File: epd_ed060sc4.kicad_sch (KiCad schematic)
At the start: 13 parts, among them J1 ED060SC4

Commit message: fix paths
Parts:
- J1: footprint (none) -> local_lib:HRS_FH26W-39S-0.3SHW(60)
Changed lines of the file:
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@@
       (effects (font (size 1.27 1.27)) (justify left))
     )
-    (property "Footprint" "" (at 173.99 82.55 0)
+    (property "Footprint" "local_lib:HRS_FH26W-39S-0.3SHW(60)" (at 173.99 82.55 0)
       (effects (font (size 1.27 1.27)) hide)
     )
-    (property "Datasheet" "" (at 173.99 82.55 0)
+    (property "Datasheet" "https://datasheetspdf.com/pdf-file/730402/PrimeView/ED060SC4/1" (at 173.99 82.55 0)
       (effects (font (size 1.27 1.27)) hide)
     )

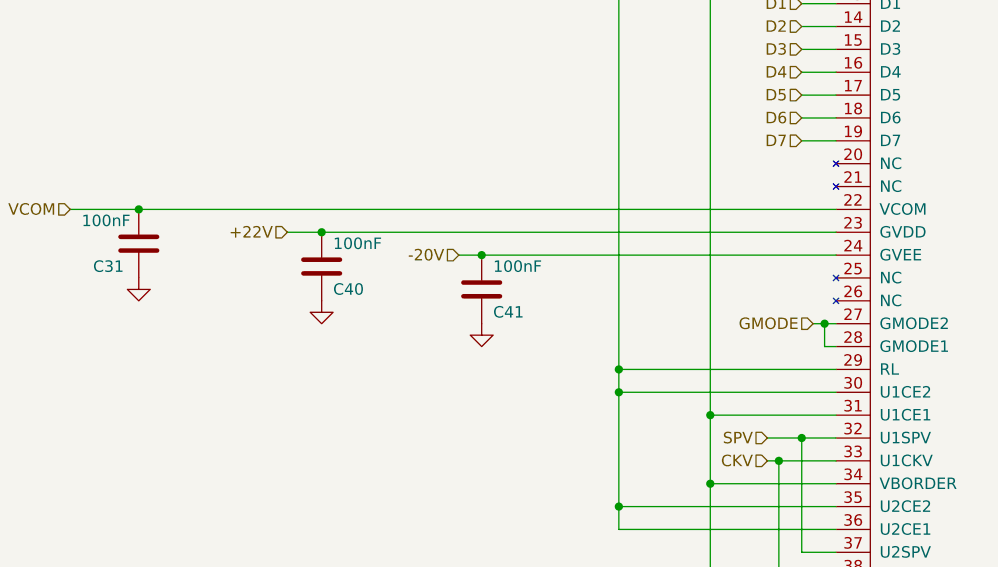
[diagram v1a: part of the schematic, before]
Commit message: Set voltage rating of capacitors
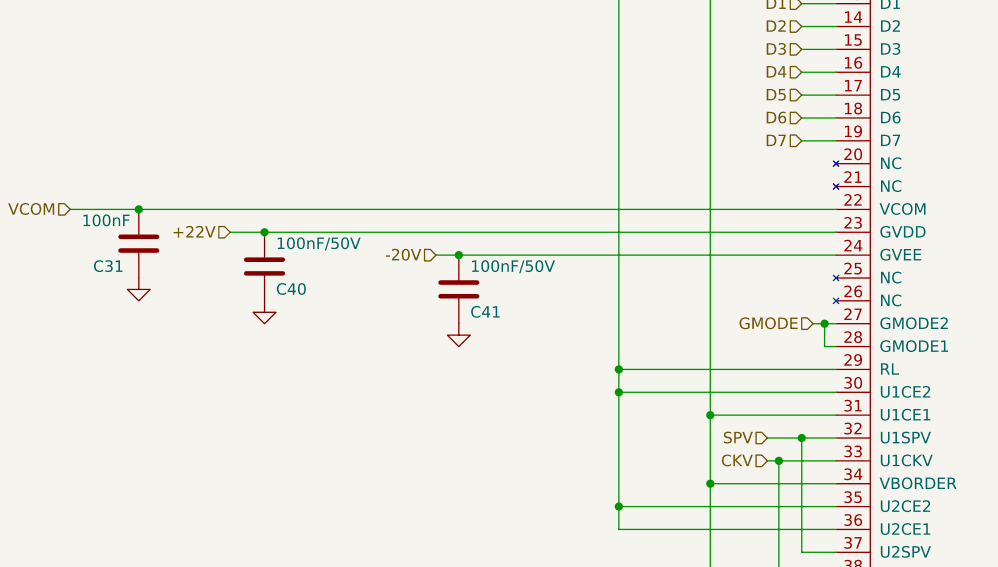
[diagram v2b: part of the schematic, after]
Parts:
- C40, C41: value 100nF -> 100nF/50V
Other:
- moved on the sheet: C40, C41
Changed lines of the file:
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@@
   (junction (at 132.08 54.61) (diameter 0) (color 0 0 0 0)
   )
+  (junction (at 127 92.71) (diameter 0) (color 0 0 0 0)
+  )
   (junction (at 144.78 120.65) (diameter 0) (color 0 0 0 0)
   )
@@
   (junction (at 116.84 54.61) (diameter 0) (color 0 0 0 0)
   )
-  (junction (at 111.76 90.17) (diameter 0) (color 0 0 0 0)
-  )
-  (junction (at 129.54 92.71) (diameter 0) (color 0 0 0 0)
+  (junction (at 105.41 90.17) (diameter 0) (color 0 0 0 0)
   )
   (junction (at 144.78 105.41) (diameter 0) (color 0 0 0 0)
   )
-  (wire (pts (xy 127 92.71) (xy 129.54 92.71))
+  (wire (pts (xy 124.46 92.71) (xy 127 92.71))
     (stroke (width 0) (type default))
   )
@@
     (stroke (width 0) (type default))
   )
-  (wire (pts (xy 129.54 92.71) (xy 168.91 92.71))
-    (stroke (width 0) (type default))
-  )
   (wire (pts (xy 124.46 54.61) (xy 132.08 54.61))
     (stroke (width 0) (type default))
@@
     (stroke (width 0) (type default))
   )
-  (wire (pts (xy 107.95 90.17) (xy 111.76 90.17))
+  (wire (pts (xy 101.6 90.17) (xy 105.41 90.17))
     (stroke (width 0) (type default))
   )
@@
     (stroke (width 0) (type default))
   )
-  (wire (pts (xy 111.76 90.17) (xy 168.91 90.17))
+  (wire (pts (xy 105.41 90.17) (xy 168.91 90.17))
     (stroke (width 0) (type default))
   )
@@
   )
   (wire (pts (xy 162.56 115.57) (xy 168.91 115.57))
+    (stroke (width 0) (type default))
+  )
+  (wire (pts (xy 127 92.71) (xy 168.91 92.71))
     (stroke (width 0) (type default))
   )
@@
     (effects (font (size 1.27 1.27)) (justify right))
   )
-  (hierarchical_label "-20V" (shape input) (at 127 92.71 180) (fields_autoplaced)
+  (hierarchical_label "-20V" (shape input) (at 124.46 92.71 180) (fields_autoplaced)
     (effects (font (size 1.27 1.27)) (justify right))
   )
@@
     (effects (font (size 1.27 1.27)) (justify right))
   )
-  (hierarchical_label "+22V" (shape input) (at 107.95 90.17 180) (fields_autoplaced)
+  (hierarchical_label "+22V" (shape input) (at 101.6 90.17 180) (fields_autoplaced)
     (effects (font (size 1.27 1.27)) (justify right))
   )
@@
     )
   )
-  (symbol (lib_id "power:GND") (at 129.54 100.33 0) (unit 1)
+  (symbol (lib_id "power:GND") (at 127 100.33 0) (unit 1)
     (in_bom yes) (on_board yes) (dnp no) (fields_autoplaced)
-    (property "Reference" "#PWR047" (at 129.54 106.68 0)
-      (effects (font (size 1.27 1.27)) hide)
-    )
-    (property "Value" "GND" (at 129.54 105.41 0)
-      (effects (font (size 1.27 1.27)) hide)
-    )
-    (property "Footprint" "" (at 129.54 100.33 0)
-      (effects (font (size 1.27 1.27)) hide)
-    )
-    (property "Datasheet" "" (at 129.54 100.33 0)
+    (property "Reference" "#PWR047" (at 127 106.68 0)
+      (effects (font (size 1.27 1.27)) hide)
+    )
+    (property "Value" "GND" (at 127 105.41 0)
+      (effects (font (size 1.27 1.27)) hide)
+    )
+    (property "Footprint" "" (at 127 100.33 0)
+      (effects (font (size 1.27 1.27)) hide)
+    )
+    (property "Datasheet" "" (at 127 100.33 0)
       (effects (font (size 1.27 1.27)) hide)
     )
@@
     )
   )
-  (symbol (lib_id "Device:C") (at 111.76 93.98 0) (unit 1)
-    (in_bom yes) (on_board yes) (dnp no)
-    (property "Reference" "C40" (at 113.03 96.52 0)
-      (effects (font (size 1.27 1.27)) (justify left))
-    )
-    (property "Value" "100nF" (at 113.03 91.44 0)
-      (effects (font (size 1.27 1.27)) (justify left))
-    )
-    (property "Footprint" "" (at 112.7252 97.79 0)
-      (effects (font (size 1.27 1.27)) hide)
-    )
-    (property "Datasheet" "~" (at 111.76 93.98 0)
+  (symbol (lib_id "Device:C") (at 105.41 93.98 0) (unit 1)
+    (in_bom yes) (on_board yes) (dnp no)
+    (property "Reference" "C40" (at 106.68 96.52 0)
+      (effects (font (size 1.27 1.27)) (justify left))
+    )
+    (property "Value" "100nF/50V" (at 106.68 91.44 0)
+      (effects (font (size 1.27 1.27)) (justify left))
+    )
+    (property "Footprint" "" (at 106.3752 97.79 0)
+      (effects (font (size 1.27 1.27)) hide)
+    )
+    (property "Datasheet" "~" (at 105.41 93.98 0)
       (effects (font (size 1.27 1.27)) hide)
     )
@@
     )
   )
-  (symbol (lib_id "power:GND") (at 111.76 97.79 0) (unit 1)
+  (symbol (lib_id "power:GND") (at 105.41 97.79 0) (unit 1)
     (in_bom yes) (on_board yes) (dnp no) (fields_autoplaced)
-    (property "Reference" "#PWR047" (at 111.76 104.14 0)
-      (effects (font (size 1.27 1.27)) hide)
-    )
-    (property "Value" "GND" (at 111.76 102.87 0)
-      (effects (font (size 1.27 1.27)) hide)
-    )
-    (property "Footprint" "" (at 111.76 97.79 0)
-      (effects (font (size 1.27 1.27)) hide)
-    )
-    (property "Datasheet" "" (at 111.76 97.79 0)
+    (property "Reference" "#PWR047" (at 105.41 104.14 0)
+      (effects (font (size 1.27 1.27)) hide)
+    )
+    (property "Value" "GND" (at 105.41 102.87 0)
+      (effects (font (size 1.27 1.27)) hide)
+    )
+    (property "Footprint" "" (at 105.41 97.79 0)
+      (effects (font (size 1.27 1.27)) hide)
+    )
+    (property "Datasheet" "" (at 105.41 97.79 0)
       (effects (font (size 1.27 1.27)) hide)
     )
@@
     )
   )
-  (symbol (lib_id "Device:C") (at 129.54 96.52 0) (unit 1)
-    (in_bom yes) (on_board yes) (dnp no)
-    (property "Reference" "C41" (at 130.81 99.06 0)
-      (effects (font (size 1.27 1.27)) (justify left))
-    )
-    (property "Value" "100nF" (at 130.81 93.98 0)
-      (effects (font (size 1.27 1.27)) (justify left))
-    )
-    (property "Footprint" "" (at 130.5052 100.33 0)
-      (effects (font (size 1.27 1.27)) hide)
-    )
-    (property "Datasheet" "~" (at 129.54 96.52 0)
-      (effects (font (size 1.27 1.27)) hide)
-    )
+  (symbol (lib_id "Device:C") (at 127 96.52 0) (unit 1)
+    (in_bom yes) (on_board yes) (dnp no)
+    (property "Reference" "C41" (at 128.27 99.06 0)
+      (effects (font (size 1.27 1.27)) (justify left))
+    )
+    (property "Value" "100nF/50V" (at 128.27 93.98 0)
+      (effects (font (size 1.27 1.27)) (justify left))
+    )
+    (property "Footprint" "" (at 127.9652 100.33 0)
+      (effects (font (size 1.27 1.27)) hide)
+    )
+    (property "Datasheet" "~" (at 127 96.52 0)
+      (effects (font (size 1.27 1.27)) hide)
+    )

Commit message: Add footprints and some labels
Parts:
- C31, C38, C39, C40, C41: footprint (none) -> Capacitor_SMD:C_0603_1608Metric
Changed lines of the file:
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@@
       (effects (font (size 1.27 1.27)) (justify left))
     )
-    (property "Footprint" "" (at 112.7252 41.91 0)
+    (property "Footprint" "Capacitor_SMD:C_0603_1608Metric" (at 112.7252 41.91 0)
       (effects (font (size 1.27 1.27)) hide)
     )
@@
       (effects (font (size 1.27 1.27)) (justify left))
     )
-    (property "Footprint" "" (at 130.5052 44.45 0)
+    (property "Footprint" "Capacitor_SMD:C_0603_1608Metric" (at 130.5052 44.45 0)
       (effects (font (size 1.27 1.27)) hide)
     )
@@
       (effects (font (size 1.27 1.27)) (justify left))
     )
-    (property "Footprint" "" (at 133.0452 62.23 0)
+    (property "Footprint" "Capacitor_SMD:C_0603_1608Metric" (at 133.0452 62.23 0)
       (effects (font (size 1.27 1.27)) hide)
     )
@@
       (effects (font (size 1.27 1.27)) (justify left))
     )
-    (property "Footprint" "" (at 102.5652 62.23 0)
+    (property "Footprint" "Capacitor_SMD:C_0603_1608Metric" (at 102.5652 62.23 0)
       (effects (font (size 1.27 1.27)) hide)
     )
@@
       (effects (font (size 1.27 1.27)) (justify left))
     )
-    (property "Footprint" "" (at 106.3752 97.79 0)
+    (property "Footprint" "Capacitor_SMD:C_0603_1608Metric" (at 106.3752 97.79 0)
       (effects (font (size 1.27 1.27)) hide)
     )
@@
       (effects (font (size 1.27 1.27)) (justify left))
     )
-    (property "Footprint" "" (at 94.9452 62.23 0)
+    (property "Footprint" "Capacitor_SMD:C_0603_1608Metric" (at 94.9452 62.23 0)
       (effects (font (size 1.27 1.27)) hide)
     )
@@
       (effects (font (size 1.27 1.27)) (justify left))
     )
-    (property "Footprint" "" (at 92.4052 95.25 0)
+    (property "Footprint" "Capacitor_SMD:C_0603_1608Metric" (at 92.4052 95.25 0)
       (effects (font (size 1.27 1.27)) hide)
     )
@@
       (effects (font (size 1.27 1.27)) (justify left))
     )
-    (property "Footprint" "" (at 127.9652 100.33 0)
+    (property "Footprint" "Capacitor_SMD:C_0603_1608Metric" (at 127.9652 100.33 0)
       (effects (font (size 1.27 1.27)) hide)
     )
@@
       (effects (font (size 1.27 1.27)) (justify left))
     )
-    (property "Footprint" "" (at 125.4252 62.23 0)
+    (property "Footprint" "Capacitor_SMD:C_0603_1608Metric" (at 125.4252 62.23 0)
       (effects (font (size 1.27 1.27)) hide)
     )
@@
       (effects (font (size 1.27 1.27)) (justify left))
     )
-    (property "Footprint" "" (at 117.8052 62.23 0)
+    (property "Footprint" "Capacitor_SMD:C_0603_1608Metric" (at 117.8052 62.23 0)
       (effects (font (size 1.27 1.27)) hide)
     )
@@
       (effects (font (size 1.27 1.27)) (justify left))
     )
-    (property "Footprint" "" (at 140.6652 62.23 0)
+    (property "Footprint" "Capacitor_SMD:C_0603_1608Metric" (at 140.6652 62.23 0)
       (effects (font (size 1.27 1.27)) hide)
     )
@@
       (effects (font (size 1.27 1.27)) (justify left))
     )
-    (property "Footprint" "" (at 110.1852 62.23 0)
-      (effects (font (size 1.27 1.27)) hide)
-    )
+    (property "Footprint" "Capacitor_SMD:C_0603_1608Metric" (at 110.1852 62.23 0)
+      (effects (font (size 1.27 1.27)) hide)
+    )

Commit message: Update EPD capacitors
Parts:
- C38, C39: Voltage (none) -> 50V
- C40, C41: value 100nF/50V -> 100nF; Voltage (none) -> 50V
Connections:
- net +15V: now also C38.1; no longer C39.1
- net -15V: now also C39.1; no longer C38.1

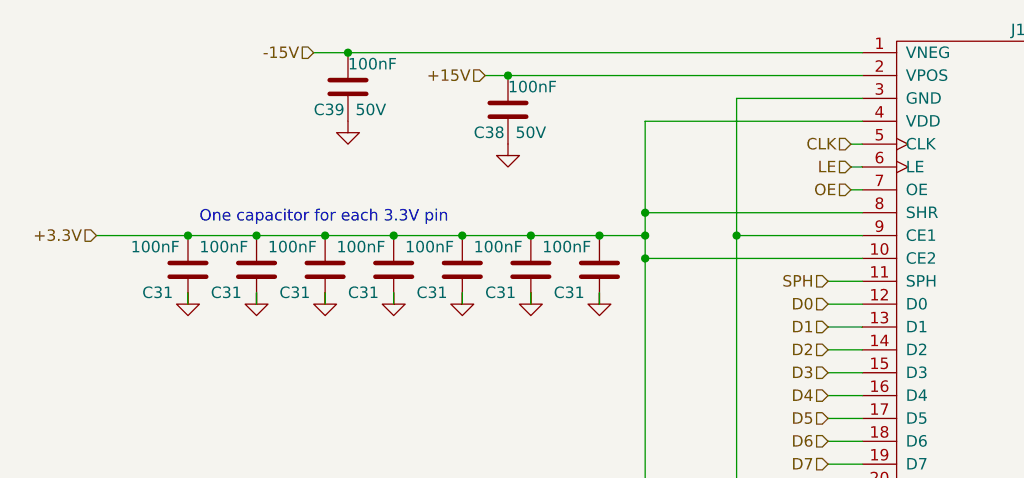
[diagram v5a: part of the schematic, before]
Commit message: Remove some capacitors for EPD
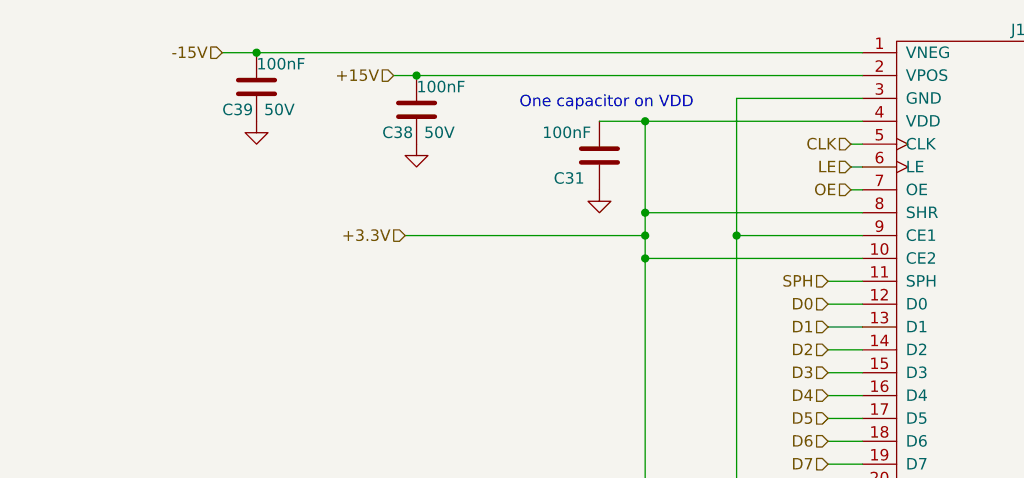
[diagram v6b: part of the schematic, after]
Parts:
- removed C31 (x7): 100nF, Capacitor_SMD:C_0603_1608Metric, symbol Device:C
- added C31: 100nF, Capacitor_SMD:C_0603_1608Metric, symbol Device:C
- C31, C38, C39, C40, C41: LCSC Part # (none) -> C1591
- J1: LCSC Part # (none) -> C92280
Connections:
- net +3.3V: now also C31.1
- net GND: now also C31.2
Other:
- note added: "One capacitor on VDD"
- note removed: "One capacitor for each 3.3V pin"
- moved on the sheet: C38, C39

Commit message: Add titles to schematics
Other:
- note added: "EPD ED060SC4"
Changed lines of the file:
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@@
     (effects (font (size 1.27 1.27)) (justify left bottom))
+  )
+  (text "EPD ED060SC4\n" (at 15.24 22.86 0)
+    (effects (font (size 5 5) (thickness 1.2) bold) (justify left bottom))
   )
   (hierarchical_label "VCOM" (shape input) (at 83.82 87.63 180) (fields_autoplaced)
